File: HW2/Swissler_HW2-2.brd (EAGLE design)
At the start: 50 x 50 mm, 22 parts, among them J1 USB-MB-H

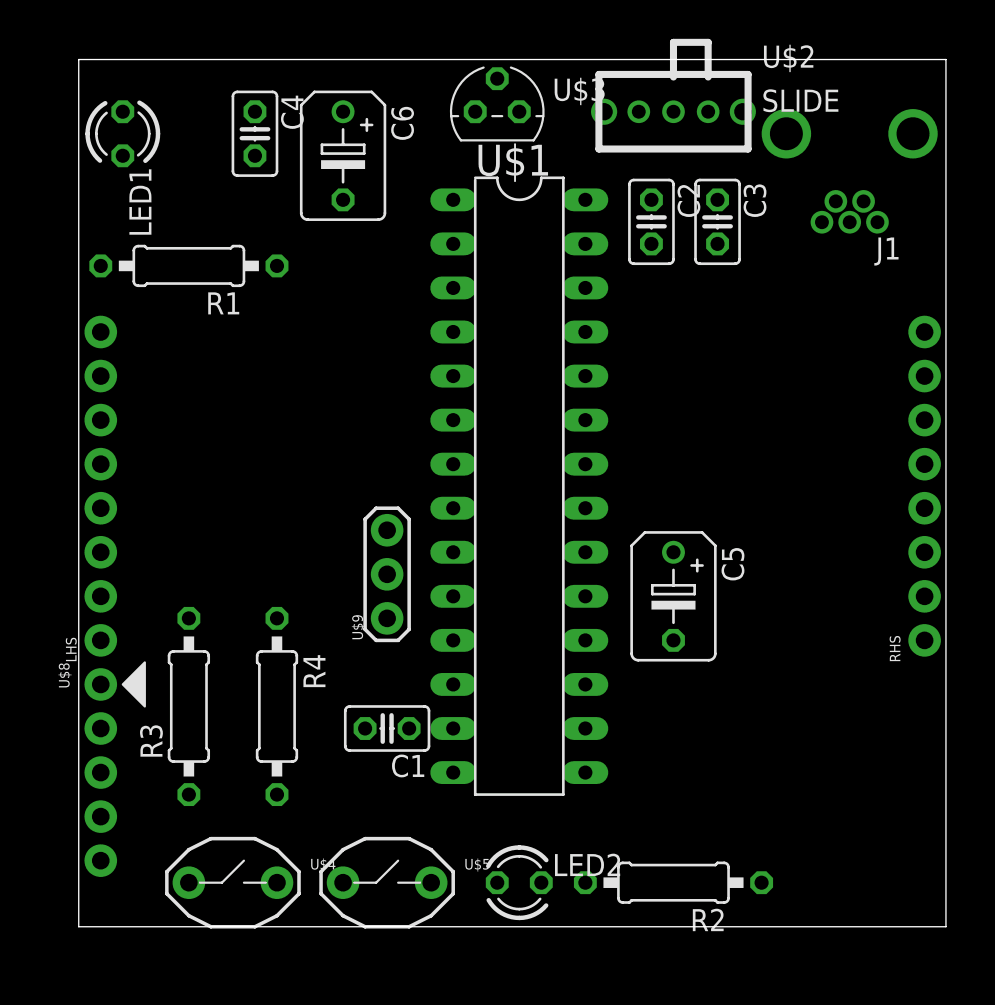
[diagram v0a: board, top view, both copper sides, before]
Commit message: New Routing Approach
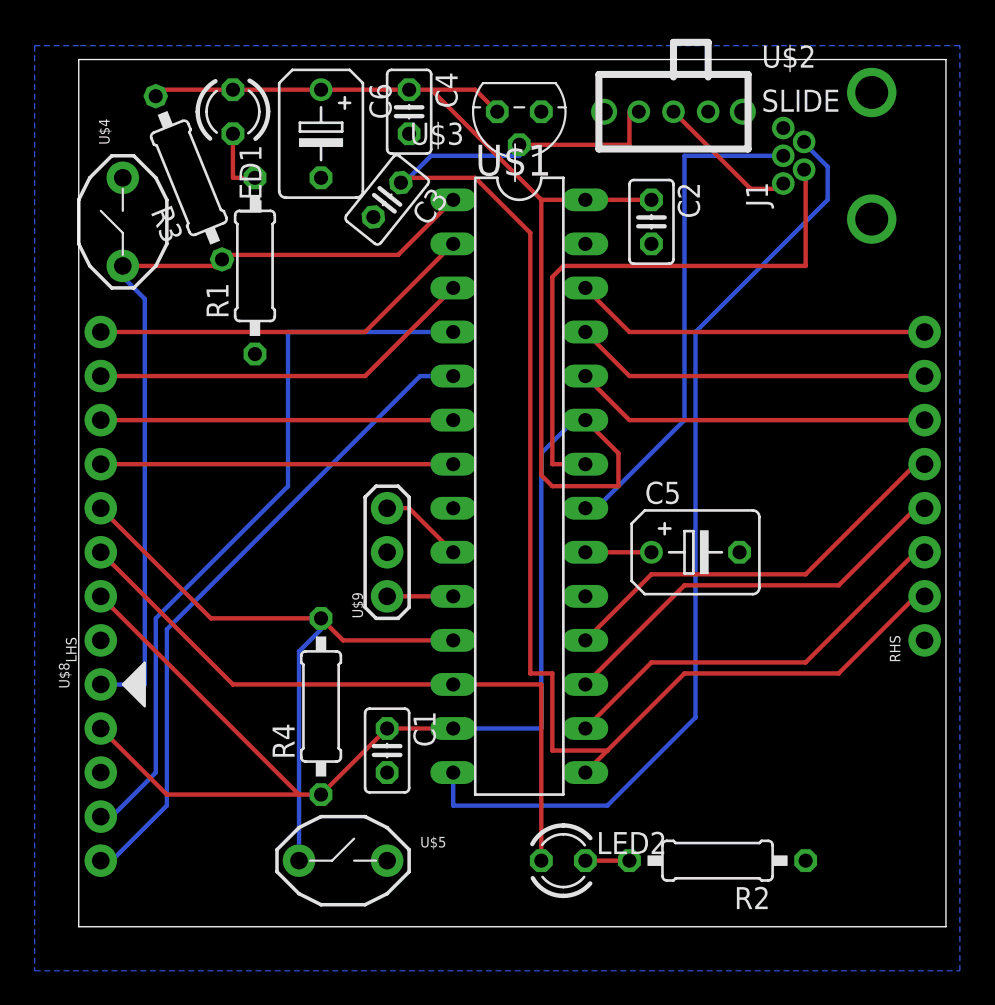
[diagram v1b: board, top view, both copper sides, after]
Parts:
- moved U$4 38.6 mm to (2.54, 40.6), turned to 90 degrees
- moved R3 30.5 mm to (6.35, 43.2), turned to 112.1 degrees
- moved C3 19.1 mm to (17.8, 41.9), turned to 231.3 degrees
- moved C4 8.98 mm to (19.1, 47.0)
- moved LED1 6.48 mm to (8.89, 47.0)
- moved R1 3.81 mm to (10.2, 38.1), turned to 90 degrees
- moved LED2 2.84 mm to (27.9, 3.81)
- moved U$5 2.84 mm to (15.2, 3.81)
- moved C5 2.84 mm to (35.6, 21.6), turned to 0 degrees
- moved R2 2.84 mm to (36.8, 3.81)
- moved R4 2.54 mm to (14.0, 12.7), turned to 90 degrees
- moved C6 1.80 mm to (14.0, 45.7)
- moved J1 1.80 mm to (45.7, 44.5), turned to 180 degrees
- moved C1 1.27 mm to (17.8, 10.2), turned to 270 degrees
- moved U$3 1.27 mm to (25.4, 47.0), turned to 180 degrees
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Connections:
- net N$1 renamed VBUS
- net N$7 renamed VCAP
- net +5V: now also U$2.1; no longer U$2.3
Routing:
- net +3V3: track 0.00 -> 125.0 mm
- net +5V: track 0.00 -> 83.8 mm
- net USBID: track 0.00 -> 54.9 mm
- net MCLR: track 0.00 -> 48.7 mm
- net PGD: track 0.00 -> 42.3 mm
- net A4/LED: track 0.00 -> 38.7 mm
- net B4/USER: track 0.00 -> 38.0 mm
- net PGC: track 0.00 -> 37.8 mm
- net D-: track 0.00 -> 33.1 mm
- net D+: track 0.00 -> 28.8 mm
- net B9: track 0.00 -> 23.8 mm
- net B8: track 0.00 -> 23.8 mm
- net B7: track 0.00 -> 23.8 mm
- net A1: track 0.00 -> 22.4 mm
- net A0: track 0.00 -> 22.4 mm
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- added copper zone on layer 16, net GND
